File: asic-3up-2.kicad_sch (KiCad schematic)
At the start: 64 parts, among them J8 Conn_01x01, J9 Conn_01x01, U57 MCP1824T-1202E/OT, U58 MCP1824T-1202E/OT, U59 MCP1824T-1202E/OT, U60 MCP1824T-0802E, U61 MCP1824T-0802E, U62 MCP1824T-0802E, U63 BM1362AC_MODE1, U64 BM1362AC_MODE0, U65 BM1362AC_MODE1

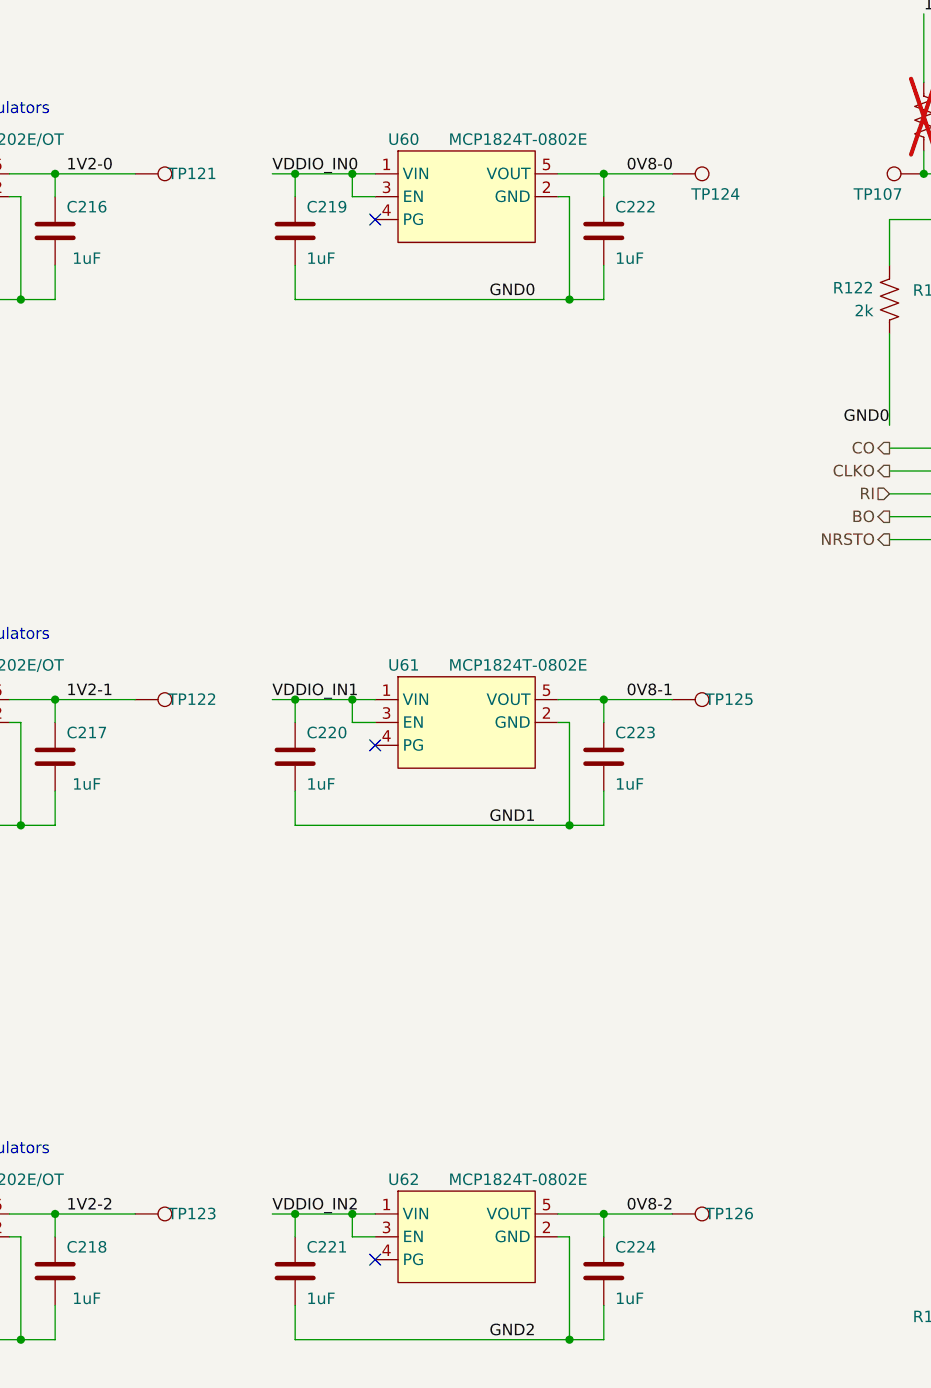
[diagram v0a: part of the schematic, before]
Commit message: remove all power pads, replace with planes, including on back layer. regenerate BOM
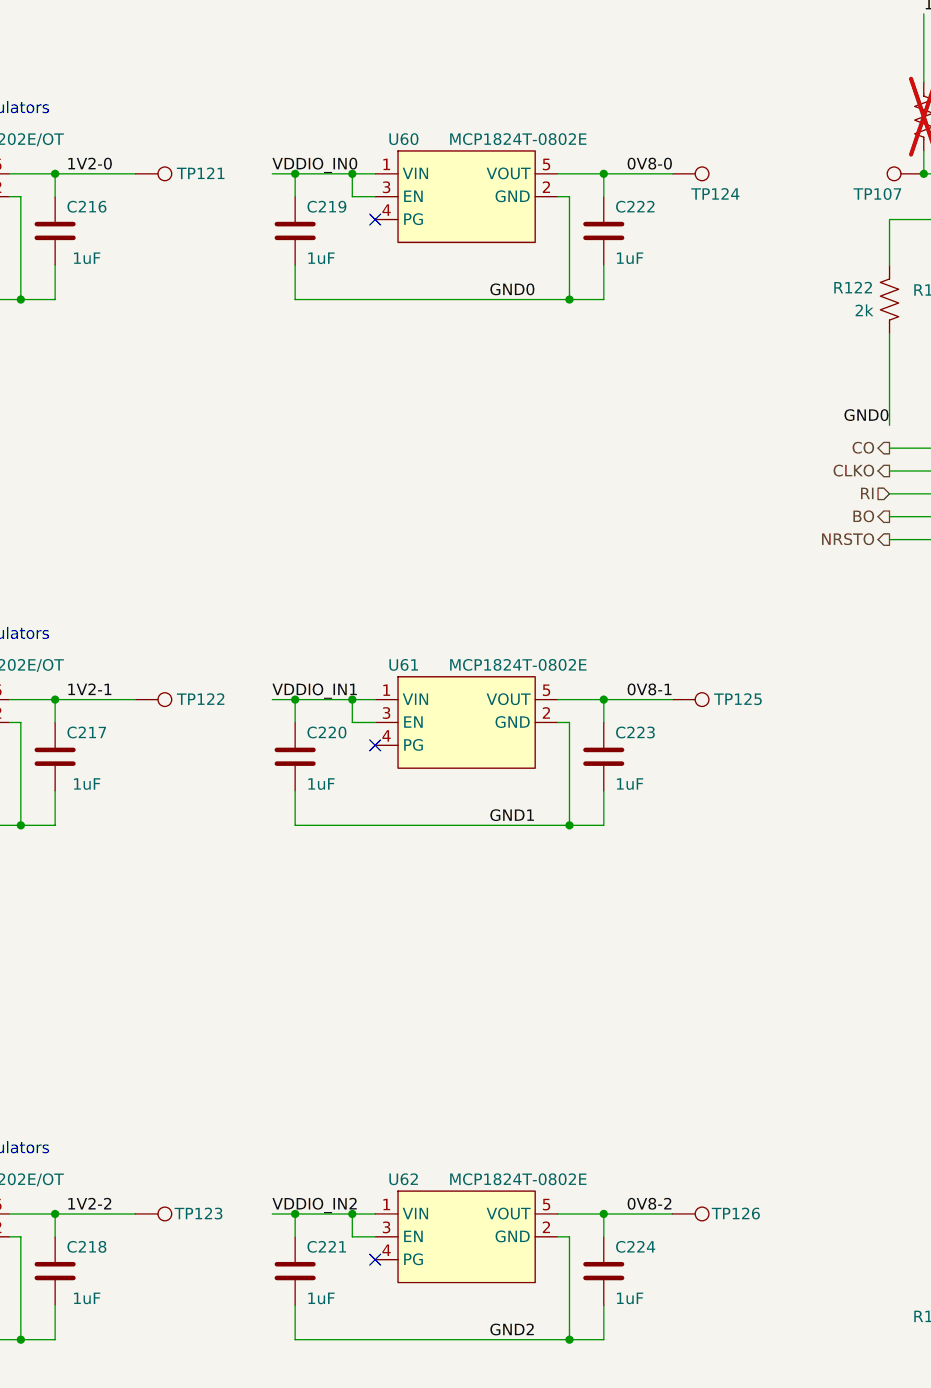
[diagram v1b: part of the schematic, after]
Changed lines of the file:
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@@
 		(dnp no)
 		(property "Reference" "TP126"
-			(at 149.86 180.34 90)
+			(at 150.622 180.34 90)
 			(effects
 				(font
@@
 		(dnp no)
 		(property "Reference" "TP125"
-			(at 149.86 123.19 90)
+			(at 150.876 123.19 90)
 			(effects
 				(font
@@
 		(dnp no)
 		(property "Reference" "TP122"
-			(at 90.17 123.19 90)
+			(at 91.186 123.19 90)
 			(effects
 				(font
@@
 		(dnp no)
 		(property "Reference" "TP121"
-			(at 90.17 64.77 90)
+			(at 91.186 64.77 90)
 			(effects
 				(font
@@
 		(dnp no)
 		(property "Reference" "TP123"
-			(at 90.17 180.34 90)
+			(at 90.932 180.34 90)
 			(effects
 				(font
